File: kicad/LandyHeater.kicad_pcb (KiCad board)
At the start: 4 copper layers, 80 x 50 mm, 139 parts, among them J1 12V IN, J2 AUTOTERM, J3 1-Wire, J4 Taster/LED, J5 USB4105-GF-A-060, Q1 2N7002K, SW1 RESET, SW2 BOOT, SW3 DIAG, U1 TPD2EUSB30DRTR, U2 TPS259470LRPWR, U3 LMR43620MSC3RPERQ1, U4 ESP32-S3-WROOM-1U-N16R8, U5 TPS3808G33DBVR, U6 RV-8263-C8, U7 TXU0202QDCURQ1, U8 TPS22945DCKR, U9 BCR421UW6Q-7

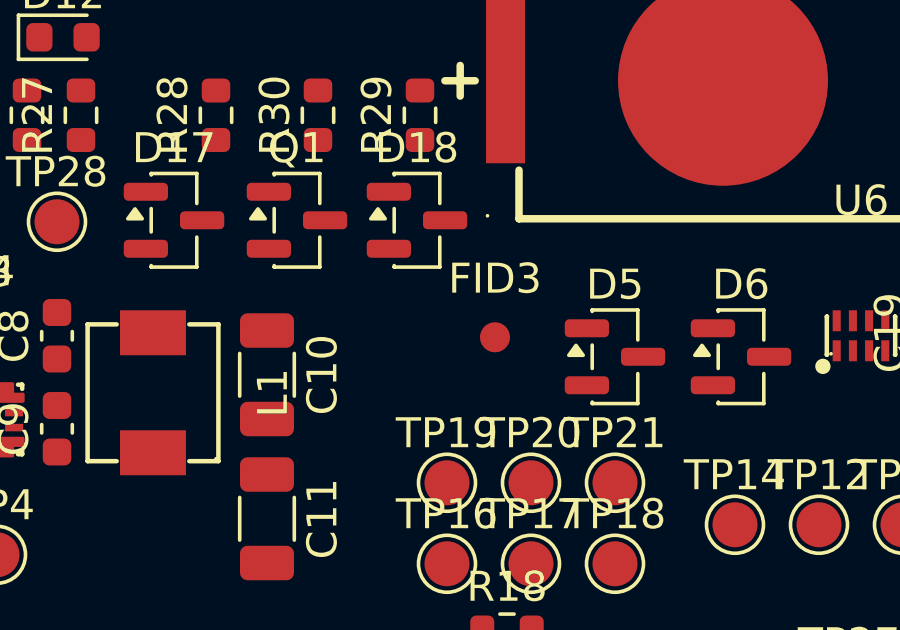
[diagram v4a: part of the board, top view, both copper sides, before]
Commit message: Validate placement with a Freerouting trial and plane-via check
- Trial routing on a copy (Freerouting 2.1.0, GND plane on L2, project
  rules for evaluation): 0 rule violations, all signals except three short
  connections at fine-pitch pads routed
- tools/check_plane_vias.py: all 107 GND/3V3/VIN_SYS pads have space for
  their own via without via-in-pad
- Move fiducial FID3 out of a routing channel found by the trial
- Record silkscreen decision E-02 (references on F.Fab, Y-08 content on silk)

Co-Authored-By: Claude Opus 5.5 <noreply@anthropic.com>
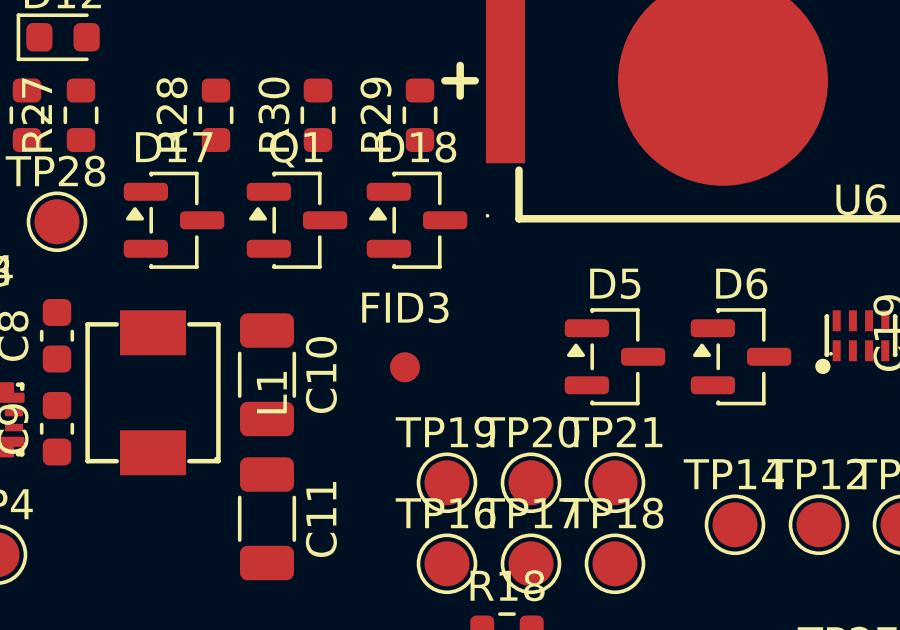
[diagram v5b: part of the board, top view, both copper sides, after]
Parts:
- moved FID3 3.16 mm to (124.0, 116.8)
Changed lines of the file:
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@@
 				(font
 					(size 1.27 1.27)
+					(thickness 0.15)
 				)
 			)
@@
 				(font
 					(size 1.27 1.27)
+					(thickness 0.15)
 				)
 			)
@@
 				(font
 					(size 1.27 1.27)
+					(thickness 0.15)
 				)
 			)
@@
 				(font
 					(size 1.27 1.27)
+					(thickness 0.15)
 				)
 			)
@@
 				(font
 					(size 1.27 1.27)
+					(thickness 0.15)
 				)
 			)
@@
 				(font
 					(size 1.27 1.27)
+					(thickness 0.15)
 				)
 			)
@@
 				(font
 					(size 1.27 1.27)
+					(thickness 0.15)
 				)
 			)
@@
 	(footprint "Fiducial_1mm_Mask2mm"
 		(layer "F.Cu")
-		(at 127 115.75)
+		(at 124 116.75)
 		(descr "Fiducial, circular marking, 1mm bare copper, 2mm soldermask opening (Level A)")
 		(tags "fiducial")
@@
 				(font
 					(size 1.27 1.27)
+					(thickness 0.15)
 				)
 			)
@@
 				(font
 					(size 1.27 1.27)
+					(thickness 0.15)
 				)
 			)
@@
 				(font
 					(size 1.27 1.27)
+					(thickness 0.15)
 				)
 			)
@@
 				(font
 					(size 1.27 1.27)
+					(thickness 0.15)
 				)
 			)
@@
 				(font
 					(size 1.27 1.27)
+					(thickness 0.15)
 				)
 			)
@@
 				(font
 					(size 1.27 1.27)
+					(thickness 0.15)
 				)
 			)
@@
 				(font
 					(size 1.27 1.27)
+					(thickness 0.15)
 				)
 			)
@@
 				(font
 					(size 1.27 1.27)
+					(thickness 0.15)
 				)
 			)
@@
 				(font
 					(size 1.27 1.27)
+					(thickness 0.15)
 				)
 			)
@@
 				(font
 					(size 1.27 1.27)
+					(thickness 0.15)
 				)
 			)
@@
 				(font
 					(size 1.27 1.27)
+					(thickness 0.15)
 				)
 			)
@@
 				(font
 					(size 1.27 1.27)
+					(thickness 0.15)
 				)
 			)
@@
 				(font
 					(size 1.27 1.27)
+					(thickness 0.15)
 				)
 			)
@@
 				(font
 					(size 1.27 1.27)
+					(thickness 0.15)
 				)
 			)
@@
 				(font
 					(size 1.27 1.27)
+					(thickness 0.15)
 				)
 			)
@@
 				(font
 					(size 1.27 1.27)
+					(thickness 0.15)
 				)
 			)
@@
 				(font
 					(size 1.27 1.27)
+					(thickness 0.15)
 				)
 			)
@@
 				(font
 					(size 1.27 1.27)
+					(thickness 0.15)
 				)
 			)
@@
 				(font
 					(size 1.27 1.27)
+					(thickness 0.15)
 				)
 			)
@@
 				(font
 					(size 1.27 1.27)
+					(thickness 0.15)
 				)
 			)
@@
 				(font
 					(size 1.27 1.27)
+					(thickness 0.15)
 				)
 			)
@@
 				(font
 					(size 1.27 1.27)
+					(thickness 0.15)
 				)
 			)
@@
 				(font
 					(size 1.27 1.27)
+					(thickness 0.15)
 				)
 			)
@@
 				(font
 					(size 1.27 1.27)
+					(thickness 0.15)
 				)
 			)
@@
 				(font
 					(size 1.27 1.27)
+					(thickness 0.15)
 				)
 			)
@@
 				(font
 					(size 1.27 1.27)
+					(thickness 0.15)
 				)
 			)
@@
 				(font
 					(size 1.27 1.27)
+					(thickness 0.15)
 				)
 			)
@@
 				(font
 					(size 1.27 1.27)
+					(thickness 0.15)
 				)
 			)
@@
 				(font
 					(size 1.27 1.27)
+					(thickness 0.15)
 				)
 			)
@@
 				(font
 					(size 1.27 1.27)
+					(thickness 0.15)
 				)
 			)
@@
 				(font
 					(size 1.27 1.27)
+					(thickness 0.15)
 				)
 			)
@@
 				(font
 					(size 1.27 1.27)
+					(thickness 0.15)
 				)
 			)
@@
 				(font
 					(size 1.27 1.27)
+					(thickness 0.15)
 				)
 			)
@@
 				(font
 					(size 1.27 1.27)
+					(thickness 0.15)
 				)
 			)
@@
 				(font
 					(size 1.27 1.27)
+					(thickness 0.15)
 				)
 			)
@@
 				(font
 					(size 1.27 1.27)
+					(thickness 0.15)
 				)
 			)
@@
 				(font
 					(size 1.27 1.27)
+					(thickness 0.15)
 				)
 			)
@@
 				(font
 					(size 1.27 1.27)
+					(thickness 0.15)
 				)
 			)
@@
 				(font
 					(size 1.27 1.27)
+					(thickness 0.15)
 				)
 			)
@@
 				(font
 					(size 1.27 1.27)
+					(thickness 0.15)
 				)
 			)
@@
 				(font
 					(size 1.27 1.27)
+					(thickness 0.15)
 				)
 			)
@@
 				(font
 					(size 1.27 1.27)
+					(thickness 0.15)
 				)
 			)
@@
 				(font
 					(size 1.27 1.27)
+					(thickness 0.15)
 				)
 			)
@@
 				(font
 					(size 1.27 1.27)
+					(thickness 0.15)
 				)
 			)
@@
 				(font
 					(size 1.27 1.27)
+					(thickness 0.15)
 				)
 			)
@@
 				(font
 					(size 1.27 1.27)
+					(thickness 0.15)
 				)
 			)
@@
 				(font
 					(size 1.27 1.27)
+					(thickness 0.15)
 				)
 			)
@@
 				(font
 					(size 1.27 1.27)
+					(thickness 0.15)
 				)
 			)
@@
 				(font
 					(size 1.27 1.27)
+					(thickness 0.15)
 				)
 			)
@@
 				(font
 					(size 1.27 1.27)
+					(thickness 0.15)
 				)
 			)
@@
 				(font
 					(size 1.27 1.27)
+					(thickness 0.15)
 				)
 			)
@@
 				(font
 					(size 1.27 1.27)
+					(thickness 0.15)
 				)
 			)
@@
 				(font
 					(size 1.27 1.27)
+					(thickness 0.15)
 				)
 			)
@@
 				(font
 					(size 1.27 1.27)
+					(thickness 0.15)
 				)
 			)
@@
 				(font
 					(size 1.27 1.27)
+					(thickness 0.15)
 				)
 			)
@@
 				(font
 					(size 1.27 1.27)
+					(thickness 0.15)
 				)
 			)
@@
 				(font
 					(size 1.27 1.27)
+					(thickness 0.15)
 				)
 			)
@@
 				(font
 					(size 1.27 1.27)
+					(thickness 0.15)
 				)
 			)
@@
 				(font
 					(size 1.27 1.27)
+					(thickness 0.15)
 				)
 			)
@@
 				(font
 					(size 1.27 1.27)
+					(thickness 0.15)
 				)
 			)
@@
 				(font
 					(size 1.27 1.27)
+					(thickness 0.15)
 				)
 			)
